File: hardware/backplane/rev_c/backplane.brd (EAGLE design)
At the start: 254 x 381 mm, 381 parts, among them J0 BACKPLANE_GENERIC_MODULE, J1 BACKPLANE_GENERIC_MODULE, J2 BACKPLANE_GENERIC_MODULE, J3 BACKPLANE_CONTROLLER_MODULE, J4 BACKPLANE_POWER_MODULE, J5 BACKPLANE_GENERIC_MODULE, J6 BACKPLANE_GENERIC_MODULE, J7 BACKPLANE_GENERIC_MODULE, J8 SCREW-TERMINAL_2_0.100, J9 SCREW-TERMINAL_2_0.100, U1 TUSB2077A, U10 SN74LVC2T45, U11 SN74LVC2T45, U12 SN74LVC2T45, U13 SN74LVC2T45, U14 SN74LVC2T45, U15 SN74LVC2T45, U16 SN74LVC2T45, U17 SN74LVC2T45, U18 SN74LVC2T45, U19 SN74LVC2T45, U2 FXMA2102, U20 TS3USB30E, U21 TS3USB30E, U22 TS3USB30E, U23 TS3USB30E, U24 TS3USB30E, U25 TS3USB30E, U26 MCP23008QFN, U27 MCP23008QFN, U28 MCP23008QFN, U29 MCP23008QFN, U3 FXMA2102, U30 MCP23008QFN, U31 MCP23008QFN, U32 MCP23008QFN, U4 FXMA2102, U5 FXMA2102, U6 FXMA2102, U7 FXMA2102, U8 SN74LVC2T45, U9 SN74LVC2T45, Y1 ABMM

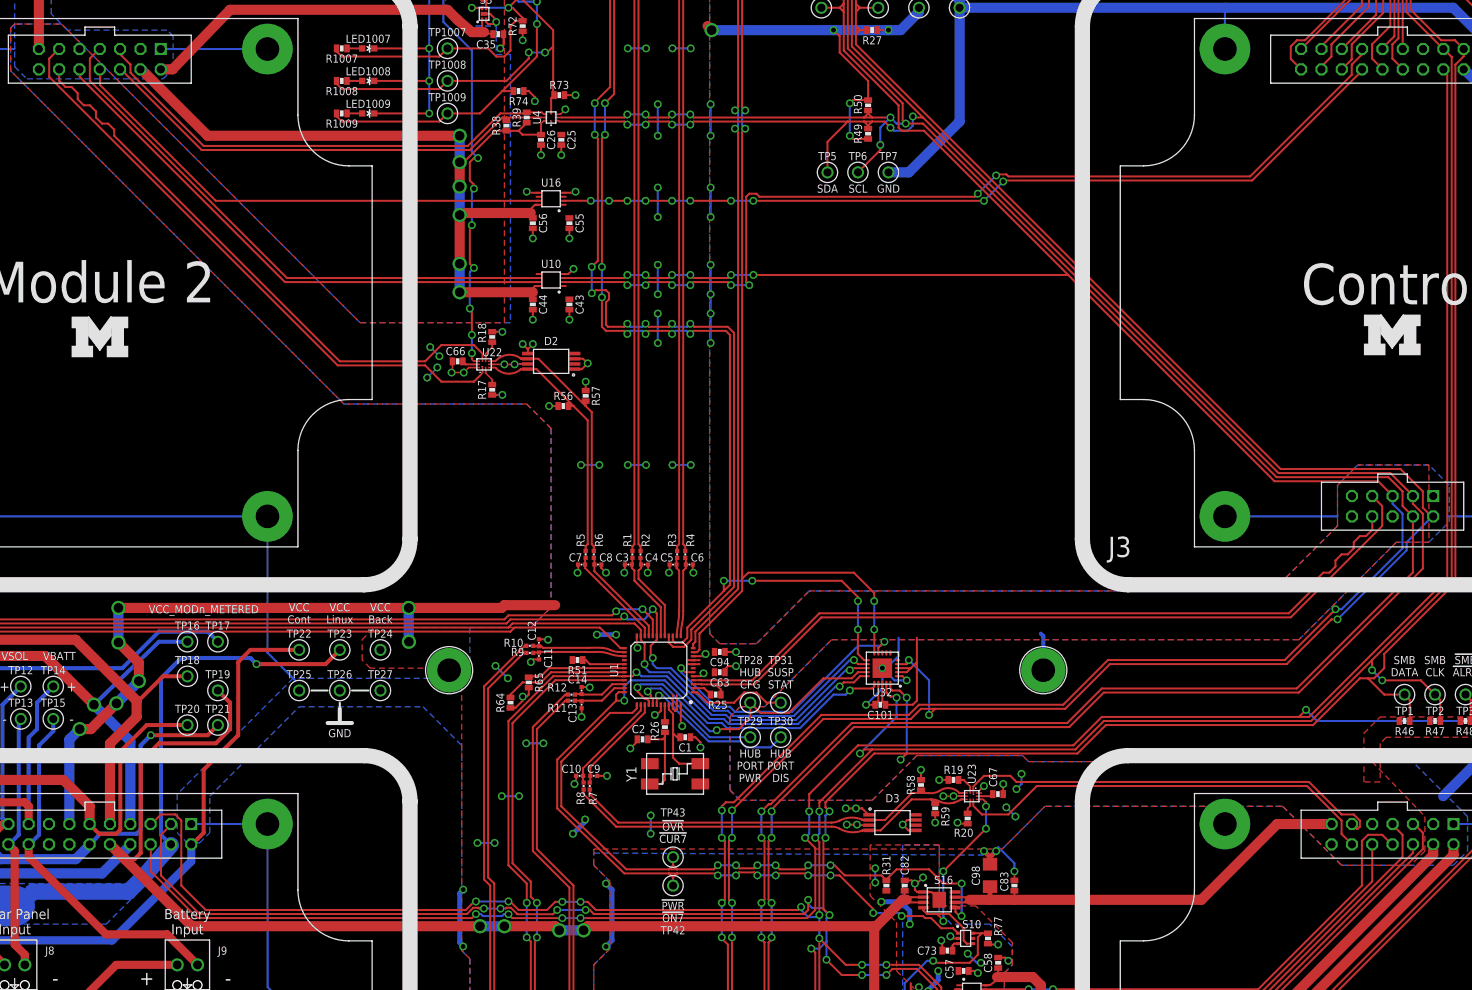
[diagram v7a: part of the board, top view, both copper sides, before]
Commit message: backplane: route !WATCHDOG
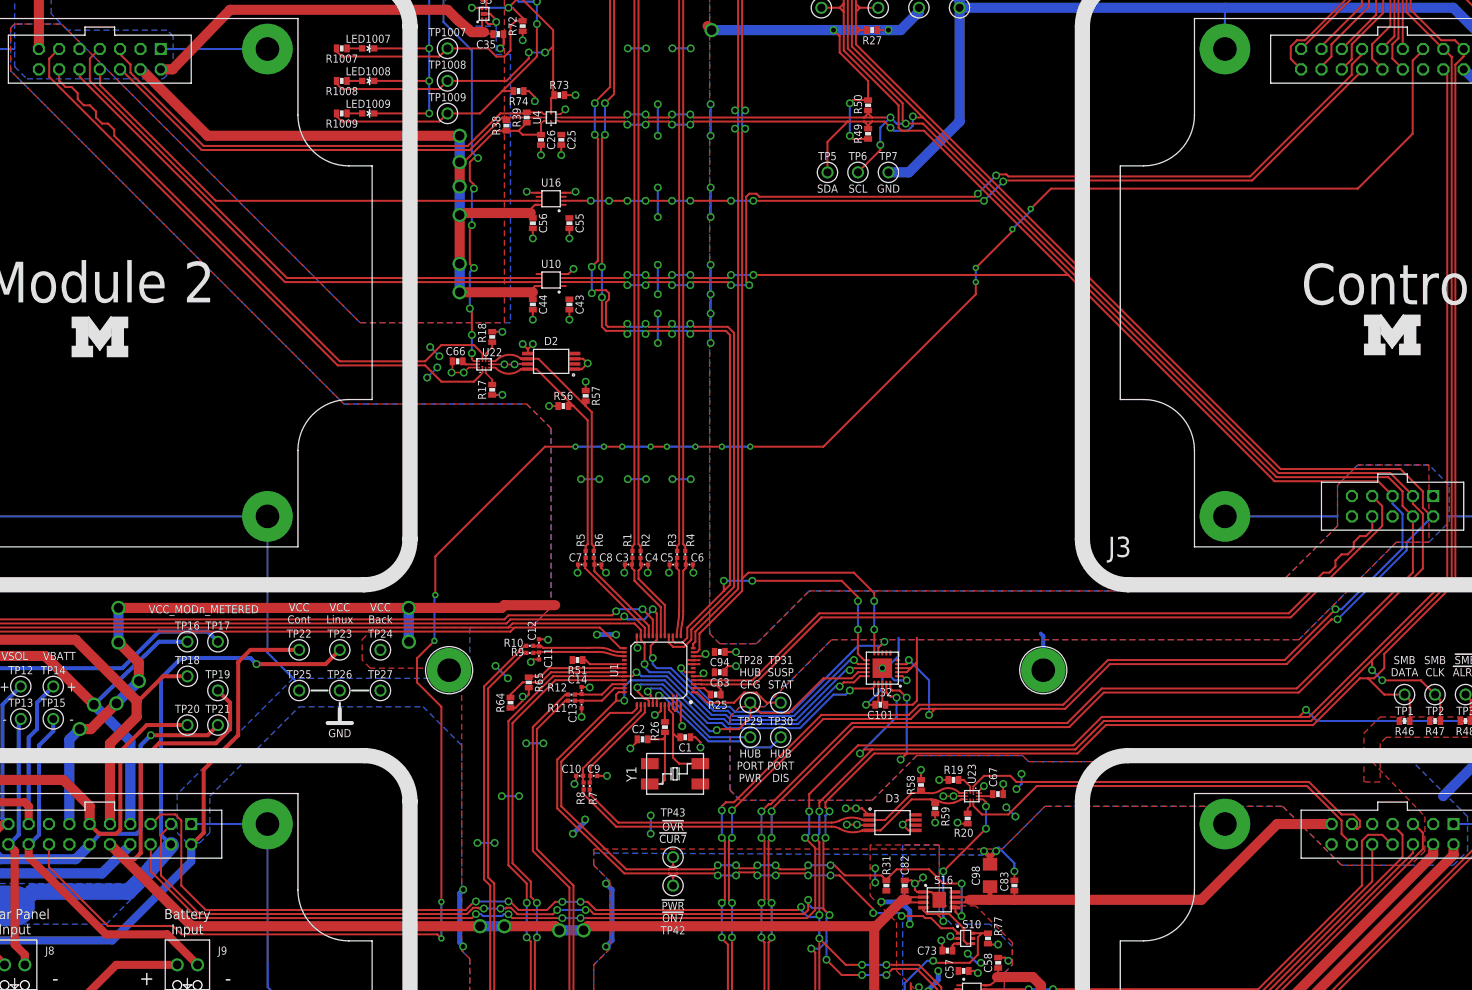
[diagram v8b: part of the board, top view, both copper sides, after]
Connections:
- new net !WATCHDOG: J3.7, J4.16
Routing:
- net !WATCHDOG: track 0.00 -> 263.0 mm, vias 0 -> 16
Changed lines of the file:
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@@
 <setting verticaltext="up"/>
 </settings>
-<grid distance="0.05" unitdist="inch" unit="inch" style="lines" multiple="1" display="yes" altdistance="0.01" altunitdist="inch" altunit="inch"/>
+<grid distance="0.01" unitdist="inch" unit="inch" style="lines" multiple="1" display="yes" altdistance="0.01" altunitdist="inch" altunit="inch"/>
 <layers>
 <layer number="1" name="Top" color="4" fill="1" visible="yes" active="yes"/>
@@
 <wire x1="110.236" y1="156.718" x2="110.236" y2="163.068" width="0.6096" layer="16"/>
 <wire x1="110.236" y1="163.068" x2="109.474" y2="163.83" width="0.6096" layer="16"/>
-<via x="117.784246875" y="216.156640625" extent="1-16" drill="0.6"/>
-<via x="120.070246875" y="216.156640625" extent="1-16" drill="0.6"/>
-<wire x1="120.070246875" y1="216.156640625" x2="117.784246875" y2="216.156640625" width="0.254" layer="16"/>
-<via x="112.196246875" y="216.156640625" extent="1-16" drill="0.6"/>
-<via x="114.482246875" y="216.156640625" extent="1-16" drill="0.6"/>
-<wire x1="114.482246875" y1="216.156640625" x2="112.196246875" y2="216.156640625" width="0.254" layer="16"/>
-<via x="106.354246875" y="216.156640625" extent="1-16" drill="0.6"/>
-<via x="108.640246875" y="216.156640625" extent="1-16" drill="0.6"/>
-<wire x1="108.640246875" y1="216.156640625" x2="106.354246875" y2="216.156640625" width="0.254" layer="16"/>
+<via x="117.784246875" y="214.378640625" extent="1-16" drill="0.6"/>
+<via x="120.070246875" y="214.378640625" extent="1-16" drill="0.6"/>
+<wire x1="120.070246875" y1="214.378640625" x2="117.784246875" y2="214.378640625" width="0.254" layer="16"/>
+<via x="112.196246875" y="214.378640625" extent="1-16" drill="0.6"/>
+<via x="114.482246875" y="214.378640625" extent="1-16" drill="0.6"/>
+<wire x1="114.482246875" y1="214.378640625" x2="112.196246875" y2="214.378640625" width="0.254" layer="16"/>
+<via x="106.354246875" y="214.378640625" extent="1-16" drill="0.6"/>
+<via x="108.640246875" y="214.378640625" extent="1-16" drill="0.6"/>
+<wire x1="108.640246875" y1="214.378640625" x2="106.354246875" y2="214.378640625" width="0.254" layer="16"/>
 <via x="117.784246875" y="268.226640625" extent="1-16" drill="0.6"/>
 <via x="120.070246875" y="268.226640625" extent="1-16" drill="0.6"/>
@@
 <wire x1="120.378" y1="191.75" x2="119.654" y2="191.75" width="0.254" layer="1"/>
 <wire x1="119.654" y1="191.75" x2="119.634" y2="191.77" width="0.254" layer="1"/>
+<wire x1="108.331" y1="194.945" x2="103.124" y2="198.628" width="0" layer="19" extent="1-1"/>
 </signal>
 <signal name="USB_SUSPEND_STATUS">
@@
 <wire x1="143.518" y1="193.302" x2="144.272" y2="194.056" width="0.254" layer="1"/>
 </signal>
+<signal name="!WATCHDOG">
+<contactref element="J4" pad="16"/>
+<contactref element="J3" pad="7"/>
+<wire x1="39.8526" y1="168.7322" x2="39.8526" y2="165.8874" width="0.254" layer="1"/>
+<wire x1="47.2186" y1="158.5214" x2="55.3466" y2="158.5214" width="0.254" layer="1"/>
+<wire x1="55.3466" y1="158.5214" x2="56.388" y2="157.48" width="0.254" layer="1"/>
+<wire x1="39.8526" y1="165.8874" x2="47.2186" y2="158.5214" width="0.254" layer="1"/>
+<wire x1="56.388" y1="157.48" x2="88.392" y2="157.48" width="0.254" layer="1"/>
+<wire x1="88.392" y1="157.48" x2="88.9" y2="156.972" width="0.254" layer="1"/>
+<via x="88.9" y="156.972" extent="1-16" drill="0.4064"/>
+<wire x1="88.9" y1="156.972" x2="88.9" y2="161.544" width="0.254" layer="16"/>
+<via x="88.9" y="161.544" extent="1-16" drill="0.4064"/>
+<wire x1="88.9" y1="161.544" x2="88.9" y2="185.928" width="0.254" layer="1"/>
+<wire x1="88.9" y1="185.928" x2="85.852" y2="188.976" width="0.254" layer="1"/>
+<wire x1="85.852" y1="188.976" x2="85.852" y2="191.98271875" width="0.254" layer="1"/>
+<wire x1="85.852" y1="191.98271875" x2="88.031640625" y2="194.162359375" width="0.254" layer="1"/>
+<via x="88.031640625" y="194.162359375" extent="1-16" drill="0.4064"/>
+<wire x1="88.031640625" y1="194.162359375" x2="88.031640625" y2="199.791640625" width="0.254" layer="16"/>
+<wire x1="88.031640625" y1="199.791640625" x2="88.138" y2="199.898" width="0.254" layer="16"/>
+<via x="88.138" y="199.898" extent="1-16" drill="0.4064"/>
+<wire x1="88.138" y1="199.898" x2="88.138" y2="204.724" width="0.254" layer="1"/>
+<wire x1="88.138" y1="204.724" x2="101.854" y2="218.44" width="0.254" layer="1"/>
+<wire x1="101.854" y1="218.44" x2="105.664" y2="218.44" width="0.254" layer="1"/>
+<via x="105.664" y="218.44" extent="1-16" drill="0.4064"/>
+<wire x1="105.664" y1="218.44" x2="109.22" y2="218.44" width="0.254" layer="16"/>
+<via x="109.22" y="218.44" extent="1-16" drill="0.4064"/>
+<wire x1="109.22" y1="218.44" x2="111.506" y2="218.44" width="0.254" layer="1"/>
+<via x="111.506" y="218.44" extent="1-16" drill="0.4064"/>
+<wire x1="111.506" y1="218.44" x2="115.062" y2="218.44" width="0.254" layer="16"/>
+<via x="115.062" y="218.44" extent="1-16" drill="0.4064"/>
+<wire x1="115.062" y1="218.44" x2="117.094" y2="218.44" width="0.254" layer="1"/>
+<via x="117.094" y="218.44" extent="1-16" drill="0.4064"/>
+<wire x1="117.094" y1="218.44" x2="120.65" y2="218.44" width="0.254" layer="16"/>
+<via x="120.65" y="218.44" extent="1-16" drill="0.4064"/>
+<wire x1="120.65" y1="218.44" x2="123.952" y2="218.44" width="0.254" layer="1"/>
+<via x="123.952" y="218.44" extent="1-16" drill="0.4064"/>
+<wire x1="123.952" y1="218.44" x2="127.508" y2="218.44" width="0.254" layer="16"/>
+<via x="127.508" y="218.44" extent="1-16" drill="0.4064"/>
+<wire x1="211.6074" y1="268.1478" x2="211.6074" y2="267.9954" width="0.254" layer="1"/>
+<wire x1="211.6074" y1="267.9954" x2="210.312" y2="266.7" width="0.254" layer="1"/>
+<wire x1="210.312" y1="266.7" x2="210.312" y2="257.556" width="0.254" layer="1"/>
+<wire x1="210.312" y1="257.556" x2="203.454" y2="250.698" width="0.254" layer="1"/>
+<wire x1="203.454" y1="250.698" x2="165.1" y2="250.698" width="0.254" layer="1"/>
+<wire x1="165.1" y1="250.698" x2="162.56" y2="248.158" width="0.254" layer="1"/>
+<via x="162.56" y="248.158" extent="1-16" drill="0.4064"/>
+<wire x1="162.56" y1="248.158" x2="162.56" y2="247.904" width="0.254" layer="16"/>
+<wire x1="162.56" y1="247.904" x2="160.274" y2="245.618" width="0.254" layer="16"/>
+<via x="160.274" y="245.618" extent="1-16" drill="0.4064"/>
+<wire x1="160.274" y1="245.618" x2="160.274" y2="245.364" width="0.254" layer="1"/>
+<wire x1="160.274" y1="245.364" x2="155.702" y2="240.792" width="0.254" layer="1"/>
+<via x="155.702" y="240.792" extent="1-16" drill="0.4064"/>
+<wire x1="155.702" y1="240.792" x2="155.702" y2="239.014" width="0.254" layer="16"/>
+<via x="155.702" y="239.014" extent="1-16" drill="0.4064"/>
+<wire x1="127.508" y1="218.44" x2="136.652" y2="218.44" width="0.254" layer="1"/>
+<wire x1="136.652" y1="218.44" x2="155.702" y2="237.49" width="0.254" layer="1"/>
+<wire x1="155.702" y1="237.49" x2="155.702" y2="239.014" width="0.254" layer="1"/>
+</signal>
 </signals>
